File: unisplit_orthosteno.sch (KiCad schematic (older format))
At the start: 55 parts, among them U1 ProMicro

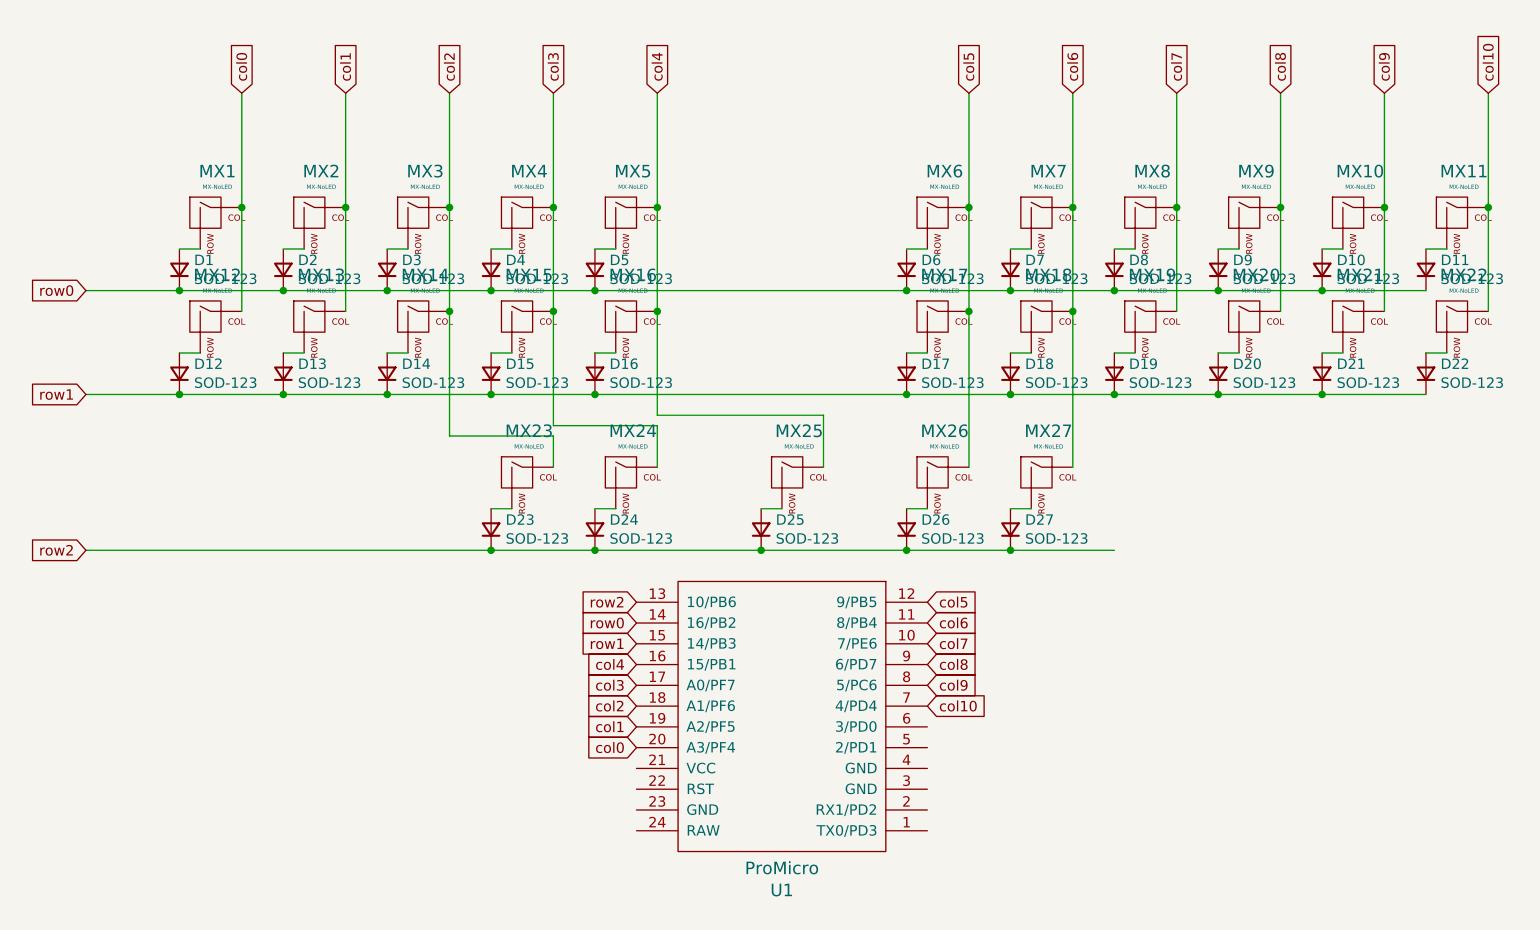
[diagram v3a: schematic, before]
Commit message: re route and change layout per suggestions from plover discord
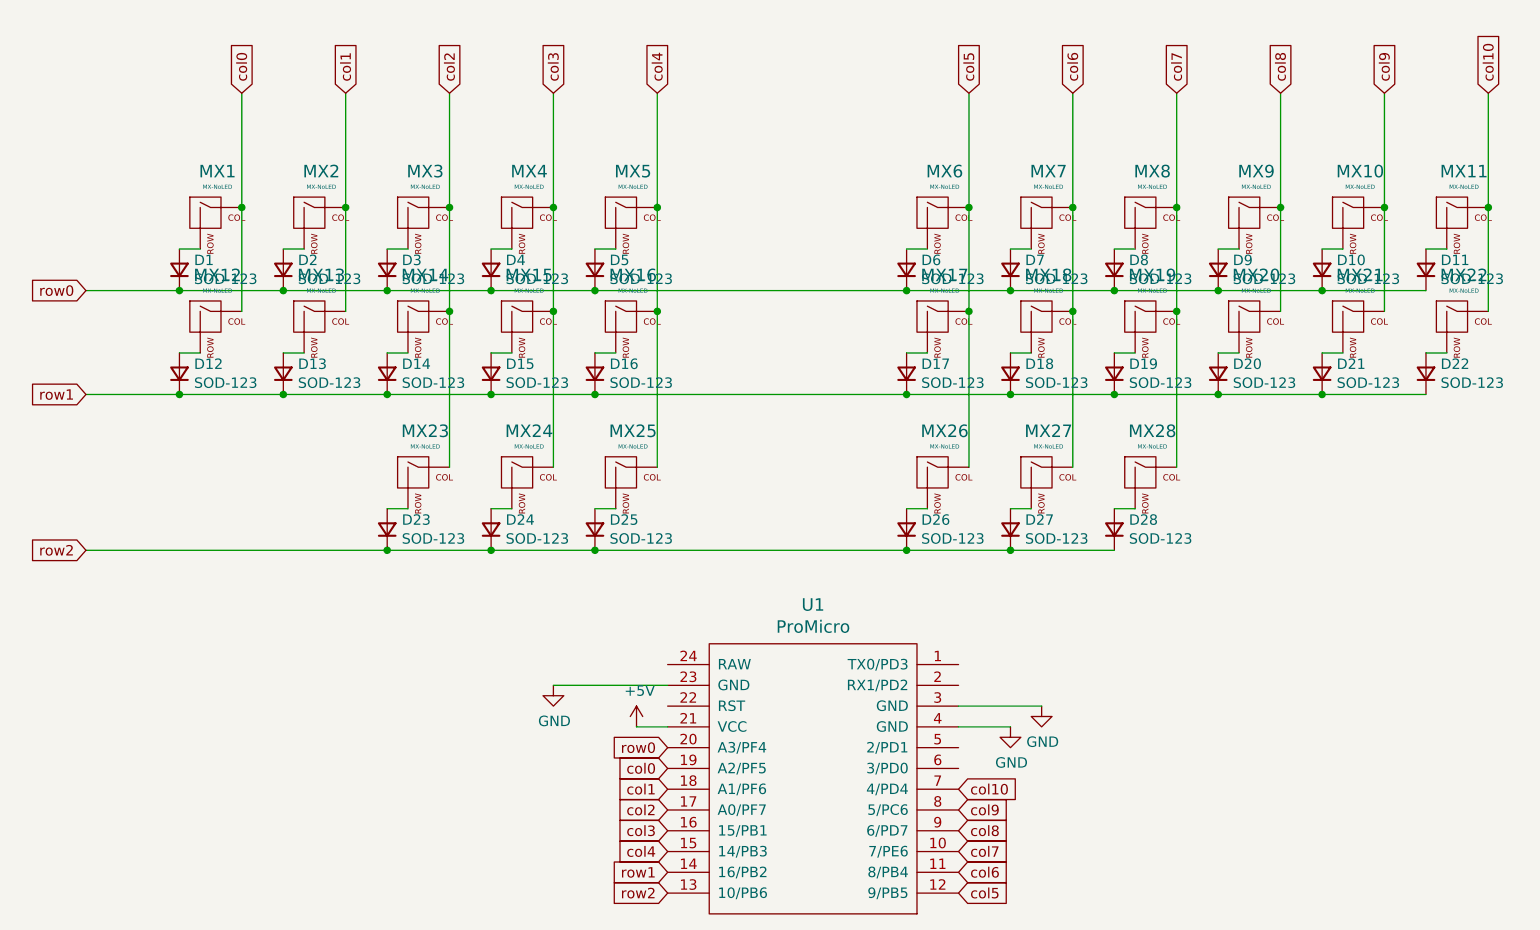
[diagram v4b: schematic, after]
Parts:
- added D28: SOD-123, Keebio-Parts:D_SOD123, symbol Device:D_Small
- added MX28: MX-NoLED, Keebio-Parts:MX-Alps-Choc-1U-NoLED, symbol MX_Alps_Hybrid:MX-NoLED
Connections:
- net col0: now also U1.19 (A2/PF5); no longer U1.20 (A3/PF4)
- net col1: now also U1.18 (A1/PF6); no longer U1.19 (A2/PF5)
- net col2: now also U1.17 (A0/PF7); no longer U1.18 (A1/PF6)
- net col3: now also U1.16 (15/PB1); no longer U1.17 (A0/PF7)
- net col4: now also U1.15 (14/PB3); no longer U1.16 (15/PB1)
- net col7: now also MX28.1 (COL)
- net row0: now also U1.20 (A3/PF4); no longer U1.14 (16/PB2)
- net row1: now also U1.14 (16/PB2); no longer U1.15 (14/PB3)
- net row2: now also D28.1 (K)
- net +5V: now reaches U1.21 (VCC)
- net GND: now reaches U1.23 (GND)
- net GND: now also U1.3 (GND), U1.4 (GND)
- new net: D28.2 (A), MX28.2 (ROW)
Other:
- moved on the sheet: D23, D24, D25, MX23, MX24, MX25, U1
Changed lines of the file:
@@
 L keebio:ProMicro U1
 U 1 1 60091C15
-P 5350 4500
-F 0 "U1" H 5350 5337 60  0000 C CNN
-F 1 "ProMicro" H 5350 5231 60  0000 C CNN
-F 2 "Keebio-Parts:ArduinoProMicro" V 6400 2000 60  0001 C CNN
-F 3 "" V 6400 2000 60  0001 C CNN
-	1    5350 4500
-	-1   0    0    1
-$EndComp
-Text GLabel 4650 4050 0    50   Input ~ 0
-row0
-Text GLabel 4650 4150 0    50   Input ~ 0
+P 5500 4800
+F 0 "U1" H 5500 5637 60  0000 C CNN
+F 1 "ProMicro" H 5500 5531 60  0000 C CNN
+F 2 "Keebio-Parts:ArduinoProMicro" V 6550 2300 60  0001 C CNN
+F 3 "" V 6550 2300 60  0001 C CNN
+	1    5500 4800
+	-1   0    0    -1
+$EndComp
+Text GLabel 4800 5250 0    50   Input ~ 0
 row1
-Text GLabel 4650 3950 0    50   Input ~ 0
+Text GLabel 4800 5350 0    50   Input ~ 0
 row2
-Text GLabel 4650 4650 0    50   Input ~ 0
+Text GLabel 4800 4750 0    50   Input ~ 0
 col0
-Text GLabel 4650 4550 0    50   Input ~ 0
+Text GLabel 4800 4850 0    50   Input ~ 0
 col1
-Text GLabel 4650 4450 0    50   Input ~ 0
+Text GLabel 4800 4950 0    50   Input ~ 0
 col2
-Text GLabel 6050 3950 2    50   Input ~ 0
+Text GLabel 6200 5350 2    50   Input ~ 0
 col5
-Text GLabel 6050 4050 2    50   Input ~ 0
+Text GLabel 6200 5250 2    50   Input ~ 0
 col6
-Text GLabel 6050 4150 2    50   Input ~ 0
+Text GLabel 6200 5150 2    50   Input ~ 0
 col7
-Text GLabel 6050 4250 2    50   Input ~ 0
+Text GLabel 6200 5050 2    50   Input ~ 0
 col8
-Text GLabel 6050 4350 2    50   Input ~ 0
+Text GLabel 6200 4950 2    50   Input ~ 0
 col9
-Text GLabel 6050 4450 2    50   Input ~ 0
+Text GLabel 6200 4850 2    50   Input ~ 0
 col10
 $Comp
 L MX_Alps_Hybrid:MX-NoLED MX?
 U 1 1 6009990C
-P 4100 3350
+P 3600 3350
 AR Path="/6008E628" Ref="MX?"  Part="1"
 AR Path="/6009990C" Ref="MX23"  Part="1"
-F 0 "MX23" H 4133 3573 60  0000 C CNN
+F 0 "MX23" H 3633 3573 60  0000 C CNN
+F 1 "MX-NoLED" H 3633 3499 20  0000 C CNN
+F 2 "Keebio-Parts:MX-Alps-Choc-1U-NoLED" H 2975 3325 60  0001 C CNN
+F 3 "" H 2975 3325 60  0001 C CNN
+	1    3600 3350
+	1    0    0    -1
+$EndComp
+$Comp
+L MX_Alps_Hybrid:MX-NoLED MX24
+U 1 1 600999EE
+P 4100 3350
+F 0 "MX24" H 4133 3573 60  0000 C CNN
 F 1 "MX-NoLED" H 4133 3499 20  0000 C CNN
 F 2 "Keebio-Parts:MX-Alps-Choc-1U-NoLED" H 3475 3325 60  0001 C CNN
 F 3 "" H 3475 3325 60  0001 C CNN
 	1    4100 3350
-	1    0    0    -1
-$EndComp
-$Comp
-L MX_Alps_Hybrid:MX-NoLED MX24
-U 1 1 600999EE
-P 4600 3350
-F 0 "MX24" H 4633 3573 60  0000 C CNN
-F 1 "MX-NoLED" H 4633 3499 20  0000 C CNN
-F 2 "Keebio-Parts:MX-Alps-Choc-1U-NoLED" H 3975 3325 60  0001 C CNN
-F 3 "" H 3975 3325 60  0001 C CNN
-	1    4600 3350
 	1    0    0    -1
 $EndComp
@@
 L Device:D_Small D23
 U 1 1 600BD975
+P 3450 3600
+F 0 "D23" V 3496 3530 50  0000 R CNN
+F 1 "SOD-123" V 3405 3530 50  0000 R CNN
+F 2 "Keebio-Parts:D_SOD123" V 3450 3600 50  0001 C CNN
+F 3 "~" V 3450 3600 50  0001 C CNN
+	1    3450 3600
+	0    -1   -1   0
+$EndComp
+$Comp
+L Device:D_Small D24
+U 1 1 600BE1C4
 P 3950 3600
-F 0 "D23" V 3996 3530 50  0000 R CNN
+F 0 "D24" V 3996 3530 50  0000 R CNN
 F 1 "SOD-123" V 3905 3530 50  0000 R CNN
 F 2 "Keebio-Parts:D_SOD123" V 3950 3600 50  0001 C CNN
 F 3 "~" V 3950 3600 50  0001 C CNN
 	1    3950 3600
-	0    -1   -1   0
-$EndComp
-$Comp
-L Device:D_Small D24
-U 1 1 600BE1C4
-P 4450 3600
-F 0 "D24" V 4496 3530 50  0000 R CNN
-F 1 "SOD-123" V 4405 3530 50  0000 R CNN
-F 2 "Keebio-Parts:D_SOD123" V 4450 3600 50  0001 C CNN
-F 3 "~" V 4450 3600 50  0001 C CNN
-	1    4450 3600
 	0    -1   -1   0
 $EndComp
@@
 $EndComp
 Wire Wire Line
+	3450 3500 3550 3500
+Wire Wire Line
 	3950 3500 4050 3500
 Wire Wire Line
-	4450 3500 4550 3500
-Wire Wire Line
 	5950 3500 6050 3500
 Wire Wire Line
@@
 Wire Wire Line
 	6950 3700 6450 3700
-Connection ~ 3950 3700
+Connection ~ 3450 3700
 Connection ~ 6450 3700
 Wire Wire Line
@@
 Text GLabel 2000 3700 0    50   Input ~ 0
 row2
-Connection ~ 4450 3700
-Wire Wire Line
-	4450 3700 3950 3700
-Wire Wire Line
-	2000 3700 3950 3700
+Wire Wire Line
+	2000 3700 3450 3700
 Connection ~ 5950 3700
-Wire Wire Line
-	5950 3700 5250 3700
 $Comp
 L MX_Alps_Hybrid:MX-NoLED MX?
 U 1 1 600EED95
-P 5400 3350
+P 4600 3350
 AR Path="/6008E628" Ref="MX?"  Part="1"
 AR Path="/600EED95" Ref="MX25"  Part="1"
-F 0 "MX25" H 5433 3573 60  0000 C CNN
-F 1 "MX-NoLED" H 5433 3499 20  0000 C CNN
-F 2 "Keebio-Parts:MX-Alps-Choc-1U-NoLED" H 4775 3325 60  0001 C CNN
-F 3 "" H 4775 3325 60  0001 C CNN
-	1    5400 3350
+F 0 "MX25" H 4633 3573 60  0000 C CNN
+F 1 "MX-NoLED" H 4633 3499 20  0000 C CNN
+F 2 "Keebio-Parts:MX-Alps-Choc-1U-NoLED" H 3975 3325 60  0001 C CNN
+F 3 "" H 3975 3325 60  0001 C CNN
+	1    4600 3350
 	1    0    0    -1
 $EndComp
@@
 L Device:D_Small D25
 U 1 1 600EF1FB
-P 5250 3600
-F 0 "D25" V 5296 3530 50  0000 R CNN
-F 1 "SOD-123" V 5205 3530 50  0000 R CNN
-F 2 "Keebio-Parts:D_SOD123" V 5250 3600 50  0001 C CNN
-F 3 "~" V 5250 3600 50  0001 C CNN
-	1    5250 3600
-	0    -1   -1   0
-$EndComp
-Wire Wire Line
-	5250 3500 5350 3500
-Connection ~ 5250 3700
-Wire Wire Line
-	5250 3700 4450 3700
+P 4450 3600
+F 0 "D25" V 4496 3530 50  0000 R CNN
+F 1 "SOD-123" V 4405 3530 50  0000 R CNN
+F 2 "Keebio-Parts:D_SOD123" V 4450 3600 50  0001 C CNN
+F 3 "~" V 4450 3600 50  0001 C CNN
+	1    4450 3600
+	0    -1   -1   0
+$EndComp
+Wire Wire Line
+	4450 3500 4550 3500
 Wire Wire Line
 	6250 3300 6250 2550
@@
 Connection ~ 6750 2550
 Wire Wire Line
-	3750 2550 3750 3150
-Wire Wire Line
-	3750 3150 4250 3150
-Wire Wire Line
-	4250 3150 4250 3300
+	4250 2550 4250 3300
+Connection ~ 4250 2550
+Wire Wire Line
+	4750 2550 4750 3300
+Connection ~ 4750 2550
+Text GLabel 4800 5050 0    50   Input ~ 0
+col3
+Text GLabel 4800 5150 0    50   Input ~ 0
+col4
+Text GLabel 4800 4650 0    50   Input ~ 0
+row0
+Wire Wire Line
+	3750 2550 3750 3300
 Connection ~ 3750 2550
-Wire Wire Line
-	4250 2550 4250 3100
-Wire Wire Line
-	4250 3100 4750 3100
-Wire Wire Line
-	4750 3100 4750 3300
-Connection ~ 4250 2550
-Wire Wire Line
-	4750 2550 4750 3050
-Wire Wire Line
-	4750 3050 5550 3050
-Wire Wire Line
-	5550 3050 5550 3300
-Connection ~ 4750 2550
-Text GLabel 4650 4350 0    50   Input ~ 0
-col3
-Text GLabel 4650 4250 0    50   Input ~ 0
-col4
+Connection ~ 3950 3700
+Wire Wire Line
+	3950 3700 3450 3700
+Wire Wire Line
+	3950 3700 4450 3700
+$Comp
+L MX_Alps_Hybrid:MX-NoLED MX28
+U 1 1 600F4962
+P 7100 3350
+F 0 "MX28" H 7133 3573 60  0000 C CNN
+F 1 "MX-NoLED" H 7133 3499 20  0000 C CNN
+F 2 "Keebio-Parts:MX-Alps-Choc-1U-NoLED" H 6475 3325 60  0001 C CNN
+F 3 "" H 6475 3325 60  0001 C CNN
+	1    7100 3350
+	1    0    0    -1
+$EndComp
+$Comp
+L Device:D_Small D28
+U 1 1 600F4C34
+P 6950 3600
+F 0 "D28" V 6996 3530 50  0000 R CNN
+F 1 "SOD-123" V 6905 3530 50  0000 R CNN
+F 2 "Keebio-Parts:D_SOD123" V 6950 3600 50  0001 C CNN
+F 3 "~" V 6950 3600 50  0001 C CNN
+	1    6950 3600
+	0    -1   -1   0
+$EndComp
+Wire Wire Line
+	6950 3500 7050 3500
+Wire Wire Line
+	7250 2550 7250 3300
+Connection ~ 7250 2550
+Connection ~ 4450 3700
+Wire Wire Line
+	4450 3700 5950 3700
+$Comp
+L power:GND #PWR?
+U 1 1 601031E0
+P 4250 4350
+F 0 "#PWR?" H 4250 4100 50  0001 C CNN
+F 1 "GND" H 4255 4177 50  0000 C CNN
+F 2 "" H 4250 4350 50  0001 C CNN
+F 3 "" H 4250 4350 50  0001 C CNN
+	1    4250 4350
+	1    0    0    -1
+$EndComp
+$Comp
+L power:GND #PWR?
+U 1 1 60103715
+P 6600 4450
+F 0 "#PWR?" H 6600 4200 50  0001 C CNN
+F 1 "GND" H 6605 4277 50  0000 C CNN
+F 2 "" H 6600 4450 50  0001 C CNN
+F 3 "" H 6600 4450 50  0001 C CNN
+	1    6600 4450
+	1    0    0    -1
+$EndComp
+$Comp
+L power:GND #PWR?
+U 1 1 60103AAE
+P 6450 4550
+F 0 "#PWR?" H 6450 4300 50  0001 C CNN
+F 1 "GND" H 6455 4377 50  0000 C CNN
+F 2 "" H 6450 4550 50  0001 C CNN
+F 3 "" H 6450 4550 50  0001 C CNN
+	1    6450 4550
+	1    0    0    -1
+$EndComp
+Wire Wire Line
+	4250 4350 4800 4350
+Wire Wire Line
+	6200 4450 6600 4450
+Wire Wire Line
+	6450 4550 6200 4550
+$Comp
+L power:+5V #PWR?
+U 1 1 6010D314
+P 4650 4550
+F 0 "#PWR?" H 4650 4400 50  0001 C CNN
+F 1 "+5V" H 4665 4723 50  0000 C CNN
+F 2 "" H 4650 4550 50  0001 C CNN
+F 3 "" H 4650 4550 50  0001 C CNN
+	1    4650 4550
+	1    0    0    -1
+$EndComp
+Wire Wire Line
+	4650 4550 4800 4550
 $EndSCHEMATC

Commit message: finalize gerbers and create bom and place files for jlcpcb
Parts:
- D1, D10, D11, D12, D13, D15, D16, D17, D18, D19, D2, D20, D21, D22, D23, D24, D25, D26, D27, D28, D3, D4, D5, D6, D7, D8, D9: LCSC (none) -> C81598
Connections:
- net +5V: no longer U1.21 (VCC)
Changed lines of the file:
@@
-$EndComp
-$Comp
-L Device:D_Small D1
-U 1 1 600ACFDD
-P 2450 2350
-F 0 "D1" V 2496 2280 50  0000 R CNN
-F 1 "SOD-123" V 2405 2280 50  0000 R CNN
-F 2 "Keebio-Parts:D_SOD123" V 2450 2350 50  0001 C CNN
-F 3 "~" V 2450 2350 50  0001 C CNN
-	1    2450 2350
-	0    -1   -1   0
 $EndComp
 $Comp
@@
 F 2 "Keebio-Parts:D_SOD123" V 2450 2850 50  0001 C CNN
 F 3 "~" V 2450 2850 50  0001 C CNN
+F 4 "C81598" V 2450 2850 50  0001 C CNN "LCSC"
 	1    2450 2850
 	0    -1   -1   0
@@
 F 2 "Keebio-Parts:D_SOD123" V 2950 2350 50  0001 C CNN
 F 3 "~" V 2950 2350 50  0001 C CNN
+F 4 "C81598" V 2950 2350 50  0001 C CNN "LCSC"
 	1    2950 2350
 	0    -1   -1   0
@@
 F 2 "Keebio-Parts:D_SOD123" V 2950 2850 50  0001 C CNN
 F 3 "~" V 2950 2850 50  0001 C CNN
+F 4 "C81598" V 2950 2850 50  0001 C CNN "LCSC"
 	1    2950 2850
 	0    -1   -1   0
@@
 F 2 "Keebio-Parts:D_SOD123" V 3450 2350 50  0001 C CNN
 F 3 "~" V 3450 2350 50  0001 C CNN
+F 4 "C81598" V 3450 2350 50  0001 C CNN "LCSC"
 	1    3450 2350
 	0    -1   -1   0
@@
 F 2 "Keebio-Parts:D_SOD123" V 3950 2350 50  0001 C CNN
 F 3 "~" V 3950 2350 50  0001 C CNN
+F 4 "C81598" V 3950 2350 50  0001 C CNN "LCSC"
 	1    3950 2350
 	0    -1   -1   0
@@
 F 2 "Keebio-Parts:D_SOD123" V 3950 2850 50  0001 C CNN
 F 3 "~" V 3950 2850 50  0001 C CNN
+F 4 "C81598" V 3950 2850 50  0001 C CNN "LCSC"
 	1    3950 2850
 	0    -1   -1   0
@@
 F 2 "Keebio-Parts:D_SOD123" V 4450 2350 50  0001 C CNN
 F 3 "~" V 4450 2350 50  0001 C CNN
+F 4 "C81598" V 4450 2350 50  0001 C CNN "LCSC"
 	1    4450 2350
 	0    -1   -1   0
@@
 F 2 "Keebio-Parts:D_SOD123" V 4450 2850 50  0001 C CNN
 F 3 "~" V 4450 2850 50  0001 C CNN
+F 4 "C81598" V 4450 2850 50  0001 C CNN "LCSC"
 	1    4450 2850
 	0    -1   -1   0
@@
 F 2 "Keebio-Parts:D_SOD123" V 5950 2350 50  0001 C CNN
 F 3 "~" V 5950 2350 50  0001 C CNN
+F 4 "C81598" V 5950 2350 50  0001 C CNN "LCSC"
 	1    5950 2350
 	0    -1   -1   0
@@
 F 2 "Keebio-Parts:D_SOD123" V 5950 2850 50  0001 C CNN
 F 3 "~" V 5950 2850 50  0001 C CNN
+F 4 "C81598" V 5950 2850 50  0001 C CNN "LCSC"
 	1    5950 2850
 	0    -1   -1   0
@@
 F 2 "Keebio-Parts:D_SOD123" V 6450 2350 50  0001 C CNN
 F 3 "~" V 6450 2350 50  0001 C CNN
+F 4 "C81598" V 6450 2350 50  0001 C CNN "LCSC"
 	1    6450 2350
 	0    -1   -1   0
@@
 F 2 "Keebio-Parts:D_SOD123" V 6450 2850 50  0001 C CNN
 F 3 "~" V 6450 2850 50  0001 C CNN
+F 4 "C81598" V 6450 2850 50  0001 C CNN "LCSC"
 	1    6450 2850
 	0    -1   -1   0
@@
 F 2 "Keebio-Parts:D_SOD123" V 6950 2350 50  0001 C CNN
 F 3 "~" V 6950 2350 50  0001 C CNN
+F 4 "C81598" V 6950 2350 50  0001 C CNN "LCSC"
 	1    6950 2350
 	0    -1   -1   0
@@
 F 2 "Keebio-Parts:D_SOD123" V 6950 2850 50  0001 C CNN
 F 3 "~" V 6950 2850 50  0001 C CNN
+F 4 "C81598" V 6950 2850 50  0001 C CNN "LCSC"
 	1    6950 2850
 	0    -1   -1   0
@@
 F 2 "Keebio-Parts:D_SOD123" V 7450 2350 50  0001 C CNN
 F 3 "~" V 7450 2350 50  0001 C CNN
+F 4 "C81598" V 7450 2350 50  0001 C CNN "LCSC"
 	1    7450 2350
 	0    -1   -1   0
@@
 F 2 "Keebio-Parts:D_SOD123" V 7450 2850 50  0001 C CNN
 F 3 "~" V 7450 2850 50  0001 C CNN
+F 4 "C81598" V 7450 2850 50  0001 C CNN "LCSC"
 	1    7450 2850
 	0    -1   -1   0
@@
 F 2 "Keebio-Parts:D_SOD123" V 7950 2350 50  0001 C CNN
 F 3 "~" V 7950 2350 50  0001 C CNN
+F 4 "C81598" V 7950 2350 50  0001 C CNN "LCSC"
 	1    7950 2350
 	0    -1   -1   0
@@
 F 2 "Keebio-Parts:D_SOD123" V 7950 2850 50  0001 C CNN
 F 3 "~" V 7950 2850 50  0001 C CNN
+F 4 "C81598" V 7950 2850 50  0001 C CNN "LCSC"
 	1    7950 2850
 	0    -1   -1   0
@@
 F 2 "Keebio-Parts:D_SOD123" V 8450 2350 50  0001 C CNN
 F 3 "~" V 8450 2350 50  0001 C CNN
+F 4 "C81598" V 8450 2350 50  0001 C CNN "LCSC"
 	1    8450 2350
 	0    -1   -1   0
@@
 F 2 "Keebio-Parts:D_SOD123" V 8450 2850 50  0001 C CNN
 F 3 "~" V 8450 2850 50  0001 C CNN
+F 4 "C81598" V 8450 2850 50  0001 C CNN "LCSC"
 	1    8450 2850
 	0    -1   -1   0
@@
 F 2 "Keebio-Parts:D_SOD123" V 3450 3600 50  0001 C CNN
 F 3 "~" V 3450 3600 50  0001 C CNN
+F 4 "C81598" V 3450 3600 50  0001 C CNN "LCSC"
 	1    3450 3600
 	0    -1   -1   0
@@
 F 2 "Keebio-Parts:D_SOD123" V 3950 3600 50  0001 C CNN
 F 3 "~" V 3950 3600 50  0001 C CNN
+F 4 "C81598" V 3950 3600 50  0001 C CNN "LCSC"
 	1    3950 3600
 	0    -1   -1   0
@@
 F 2 "Keebio-Parts:D_SOD123" V 5950 3600 50  0001 C CNN
 F 3 "~" V 5950 3600 50  0001 C CNN
+F 4 "C81598" V 5950 3600 50  0001 C CNN "LCSC"
 	1    5950 3600
 	0    -1   -1   0
@@
 F 2 "Keebio-Parts:D_SOD123" V 6450 3600 50  0001 C CNN
 F 3 "~" V 6450 3600 50  0001 C CNN
+F 4 "C81598" V 6450 3600 50  0001 C CNN "LCSC"
 	1    6450 3600
 	0    -1   -1   0
@@
 F 2 "Keebio-Parts:D_SOD123" V 4450 3600 50  0001 C CNN
 F 3 "~" V 4450 3600 50  0001 C CNN
+F 4 "C81598" V 4450 3600 50  0001 C CNN "LCSC"
 	1    4450 3600
 	0    -1   -1   0
@@
 F 2 "Keebio-Parts:D_SOD123" V 6950 3600 50  0001 C CNN
 F 3 "~" V 6950 3600 50  0001 C CNN
+F 4 "C81598" V 6950 3600 50  0001 C CNN "LCSC"
 	1    6950 3600
 	0    -1   -1   0
@@
 	4450 3700 5950 3700
 $Comp
-L power:GND #PWR?
+L power:GND #PWR0101
 U 1 1 601031E0
 P 4250 4350
-F 0 "#PWR?" H 4250 4100 50  0001 C CNN
+F 0 "#PWR0101" H 4250 4100 50  0001 C CNN
 F 1 "GND" H 4255 4177 50  0000 C CNN
 F 2 "" H 4250 4350 50  0001 C CNN
@@
 $EndComp
 $Comp
-L power:GND #PWR?
+L power:GND #PWR0102
 U 1 1 60103715
 P 6600 4450
-F 0 "#PWR?" H 6600 4200 50  0001 C CNN
+F 0 "#PWR0102" H 6600 4200 50  0001 C CNN
 F 1 "GND" H 6605 4277 50  0000 C CNN
 F 2 "" H 6600 4450 50  0001 C CNN
@@
 $EndComp
 $Comp
-L power:GND #PWR?
+L power:GND #PWR0103
 U 1 1 60103AAE
 P 6450 4550
-F 0 "#PWR?" H 6450 4300 50  0001 C CNN
+F 0 "#PWR0103" H 6450 4300 50  0001 C CNN
 F 1 "GND" H 6455 4377 50  0000 C CNN
 F 2 "" H 6450 4550 50  0001 C CNN
@@
 	6450 4550 6200 4550
 $Comp
-L power:+5V #PWR?
+L power:+5V #PWR0104
 U 1 1 6010D314
 P 4650 4550
-F 0 "#PWR?" H 4650 4400 50  0001 C CNN
+F 0 "#PWR0104" H 4650 4400 50  0001 C CNN
 F 1 "+5V" H 4665 4723 50  0000 C CNN
 F 2 "" H 4650 4550 50  0001 C CNN
@@
 	1    0    0    -1
 $EndComp
-Wire Wire Line
-	4650 4550 4800 4550
+$Comp
+L Device:D_Small D1
+U 1 1 600ACFDD
+P 2450 2350
+F 0 "D1" V 2496 2280 50  0000 R CNN
+F 1 "SOD-123" V 2405 2280 50  0000 R CNN
+F 2 "Keebio-Parts:D_SOD123" V 2450 2350 50  0001 C CNN
+F 3 "~" V 2450 2350 50  0001 C CNN
+F 4 "C81598" V 2450 2350 50  0001 C CNN "LCSC"
+	1    2450 2350
+	0    -1   -1   0
+$EndComp
 $EndSCHEMATC
